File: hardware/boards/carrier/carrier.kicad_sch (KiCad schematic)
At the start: 21 parts, among them J1 XT30PW(2+2), U2 LM5163DDAR

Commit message: Add INA bypass and CAN differential pair rules
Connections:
- net CANH_BUS renamed CAN_BUS_P
- net CANL_BUS renamed CAN_BUS_N
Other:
- sheet Protected Power and Controls ports: added CAN_BUS_N, CAN_BUS_P; removed CANH_BUS, CANL_BUS
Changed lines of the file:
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@@
 		)
 	)
-	(label "CANL_BUS"
+	(label "CAN_BUS_N"
 		(at 180 205.56 180)
 		(effects
@@
 		)
 	)
-	(label "CANL_BUS"
+	(label "CAN_BUS_N"
 		(at 39.37 52.07 180)
 		(effects
@@
 		)
 	)
-	(label "CANH_BUS"
+	(label "CAN_BUS_P"
 		(at 180 210.64 180)
 		(effects
@@
 		)
 	)
-	(label "CANH_BUS"
+	(label "CAN_BUS_P"
 		(at 39.37 54.61 180)
 		(effects
@@
 		)
 	)
-	(label "CANH_BUS"
+	(label "CAN_BUS_P"
 		(at 66.04 41.91 180)
 		(effects
@@
 		)
 	)
-	(label "CANL_BUS"
+	(label "CAN_BUS_N"
 		(at 66.04 64.77 180)
 		(effects
@@
 			)
 		)
-		(pin "CANL_BUS" bidirectional
+		(pin "CAN_BUS_N" bidirectional
 			(at 180 205.56 180)
 			(effects
@@
 			)
 		)
-		(pin "CANH_BUS" bidirectional
+		(pin "CAN_BUS_P" bidirectional
 			(at 180 210.64 180)
 			(effects

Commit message: Checkpoint updated carrier placement and CAN routing
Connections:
- net CAN_BUS_N: now also J1.4 (Pin_4); no longer J1.3 (Pin_3)
- net CAN_BUS_P: now also J1.3 (Pin_3); no longer J1.4 (Pin_4)
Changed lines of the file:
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@@
+		)
+	)
+	(label "CAN_BUS_N"
+		(at 39.37 54.61 180)
+		(effects
+			(font
+				(size 1.27 1.27)
+			)
+			(justify right bottom)
 		)
 	)
@@
 		)
 	)
-	(label "CAN_BUS_N"
-		(at 39.37 52.07 180)
-		(effects
-			(font
-				(size 1.27 1.27)
-			)
-			(justify right bottom)
-		)
-	)
 	(label "BUCK_FB"
 		(at 58.42 161.29 0)
@@
 	)
 	(label "CAN_BUS_P"
-		(at 39.37 54.61 180)
-		(effects
-			(font
-				(size 1.27 1.27)
-			)
-			(justify right bottom)
-		)
-	)
-	(label "CAN_BUS_P"
 		(at 66.04 41.91 180)
 		(effects
@@
 		(effects
 			(font
+				(size 1.27 1.27)
+			)
+			(justify right bottom)
+		)
+	)
+	(label "CAN_BUS_P"
+		(at 39.37 52.07 180)
+		(effects
+			(font

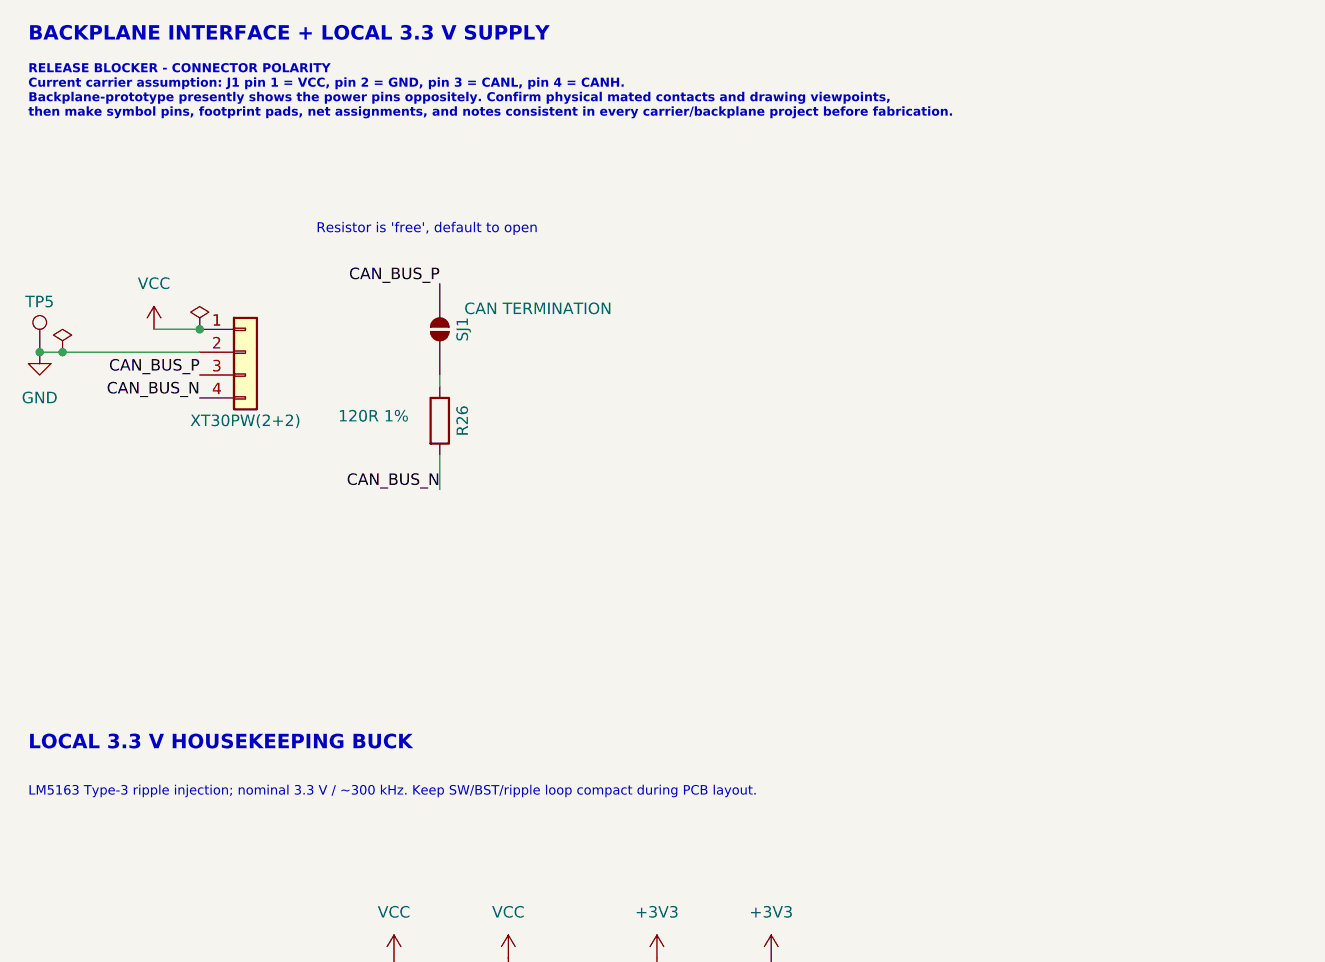
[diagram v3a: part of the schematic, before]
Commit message: Add 0.20 mm-clearance MSOP-10 footprint
Use a project-local MSOP-10 footprint for U3, document the 2 oz fabrication rationale, and include the pending carrier CAN, LED resistor, and choke footprint updates.
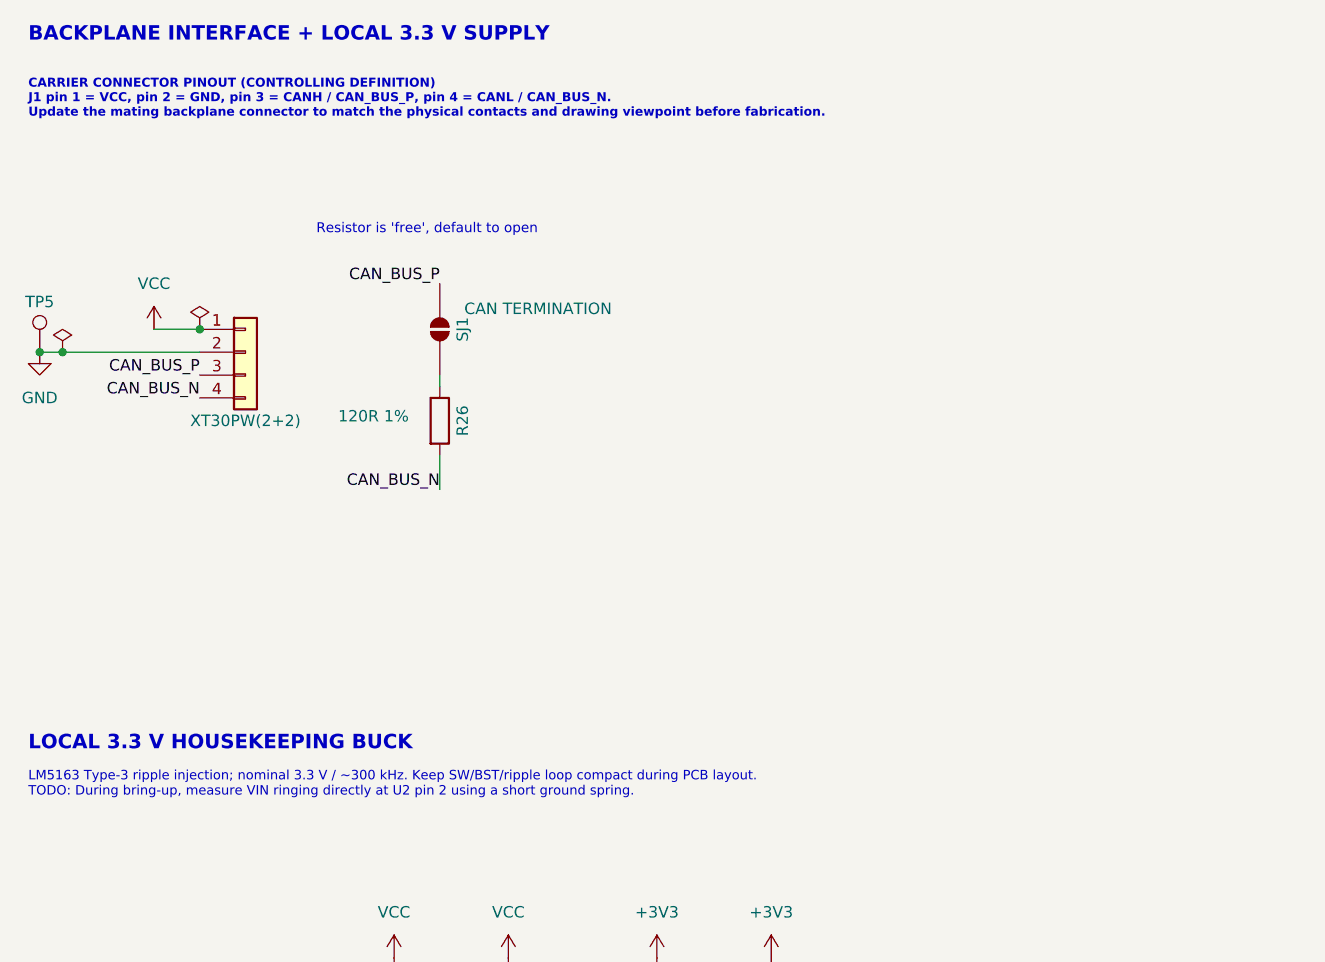
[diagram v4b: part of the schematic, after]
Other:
- note added: "CARRIER CONNECTOR PINOUT (CONTROLLING DEFINITION) J1 pin 1 = VCC, pin 2 = GND, pin 3 = CANH / CAN_BUS_P, pin 4 = CANL / CAN_BUS_N. Update the mating backplane connector to match the physical contacts and drawing viewpoint before fabrication."
- note added: "LM5163 Type-3 ripple injection; nominal 3.3 V / ~300 kHz. Keep SW/BST/ripple loop compact during PCB layout. TODO: During bring-up, measure VIN ringing directly at U2 pin 2 using a short ground spring."
- note removed: "LM5163 Type-3 ripple injection; nominal 3.3 V / ~300 kHz. Keep SW/BST/ripple loop compact during PCB layout."
- note removed: "RELEASE BLOCKER - CONNECTOR POLARITY Current carrier assumption: J1 pin 1 = VCC, pin 2 = GND, pin 3 = CANL, pin 4 = CANH. Backplane-prototype presently shows the power pins oppositely. Confirm physical mated contacts and drawing viewpoints, then make symbol pins, footprint pads, net assignments, and notes consistent in every carrier/backplane project before fabrication."
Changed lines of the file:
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@@
 		)
 	)
-	(text "LM5163 Type-3 ripple injection; nominal 3.3 V / ~300 kHz. Keep SW/BST/ripple loop compact during PCB layout."
+	(text "LM5163 Type-3 ripple injection; nominal 3.3 V / ~300 kHz. Keep SW/BST/ripple loop compact during PCB layout.\nTODO: During bring-up, measure VIN ringing directly at U2 pin 2 using a short ground spring."
 		(exclude_from_sim no)
 		(at 20.32 99.06 0)
@@
 		)
 	)
-	(text "RELEASE BLOCKER - CONNECTOR POLARITY\nCurrent carrier assumption: J1 pin 1 = VCC, pin 2 = GND, pin 3 = CANL, pin 4 = CANH.\nBackplane-prototype presently shows the power pins oppositely. Confirm physical mated contacts and drawing viewpoints,\nthen make symbol pins, footprint pads, net assignments, and notes consistent in every carrier/backplane project before fabrication."
+	(text "CARRIER CONNECTOR PINOUT (CONTROLLING DEFINITION)\nJ1 pin 1 = VCC, pin 2 = GND, pin 3 = CANH / CAN_BUS_P, pin 4 = CANL / CAN_BUS_N.\nUpdate the mating backplane connector to match the physical contacts and drawing viewpoint before fabrication."
 		(exclude_from_sim no)
 		(at 20.32 23.622 0)

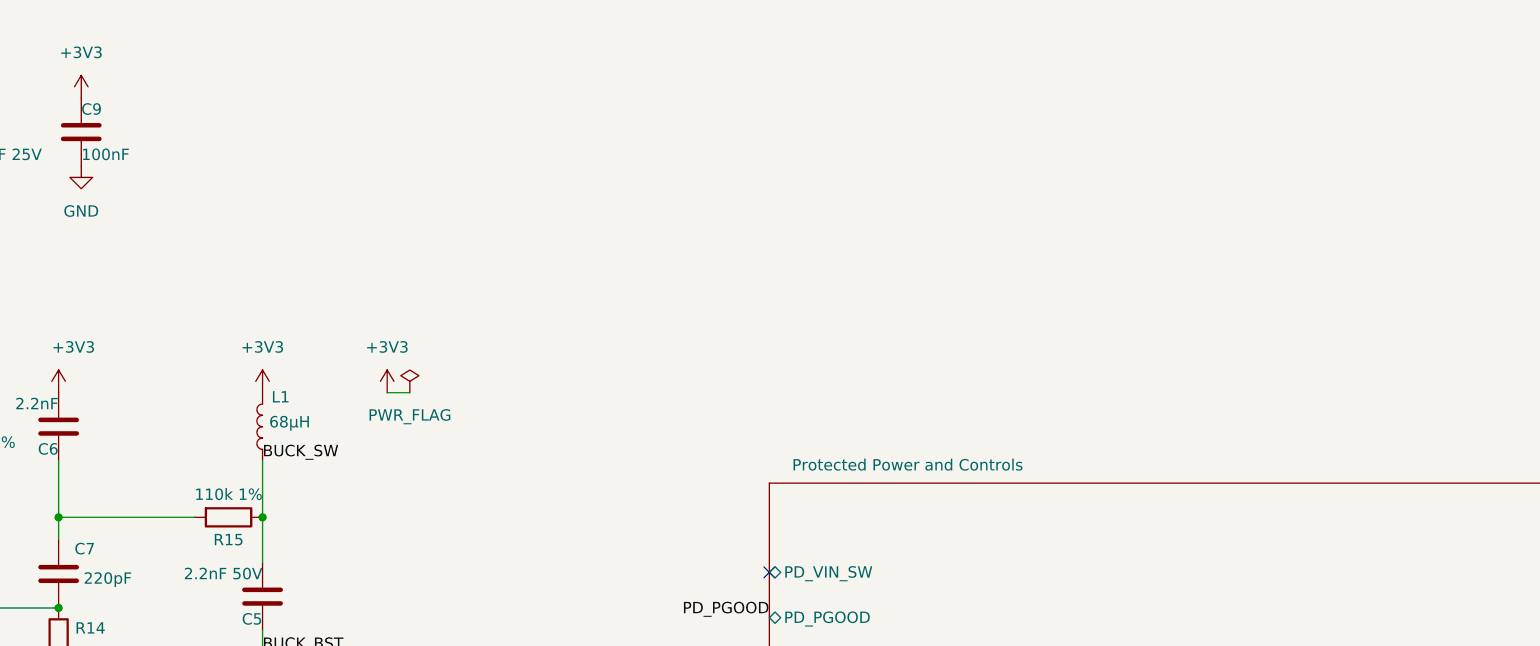
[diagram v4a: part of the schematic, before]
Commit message: add carrier bring-up testpoints
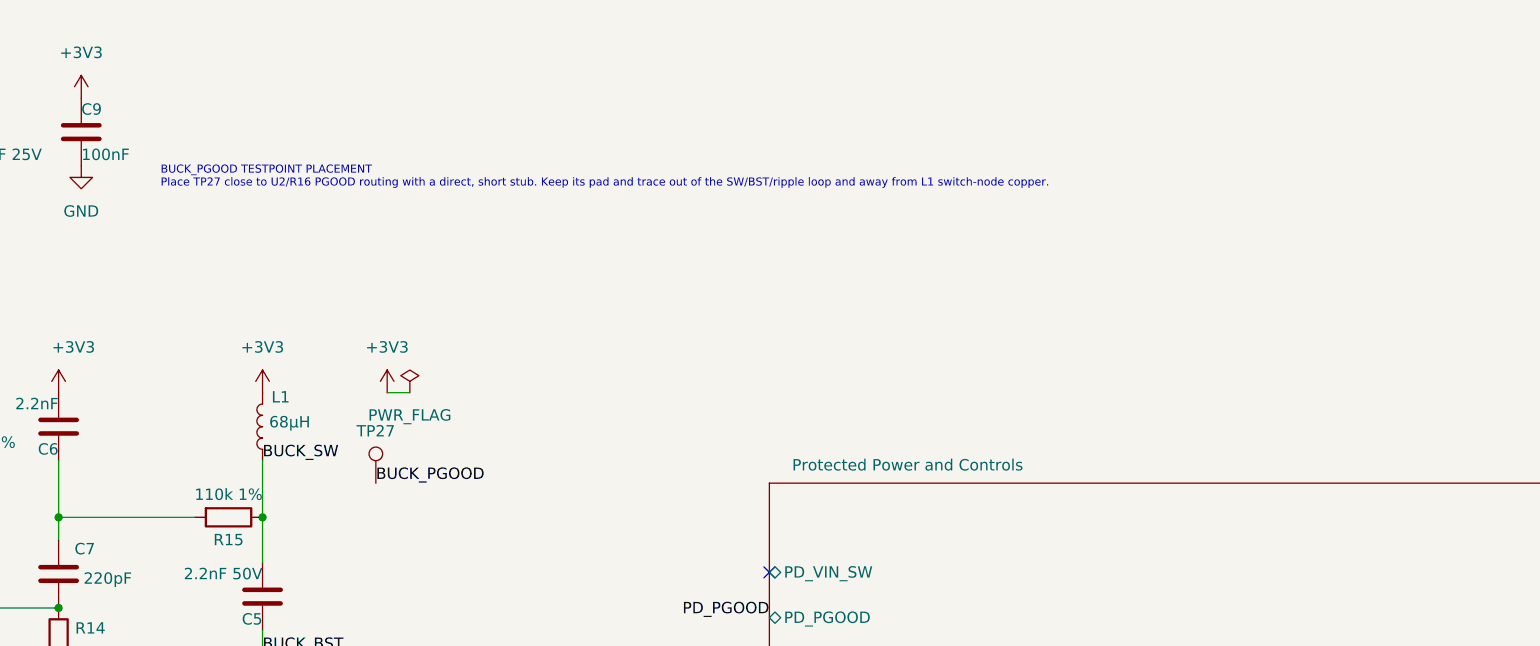
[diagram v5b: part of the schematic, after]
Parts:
- added TP27: BUCK_PGOOD, TestPoint:TestPoint_Pad_D1.5mm, symbol Connector:TestPoint
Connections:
- net BUCK_PGOOD: now also TP27.1
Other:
- note added: "BUCK_PGOOD TESTPOINT PLACEMENT Place TP27 close to U2/R16 PGOOD routing with a direct, short stub. Keep its pad and trace out of the SW/BST/ripple loop and away from L1 switch-node copper."
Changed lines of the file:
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@@
+		)
+	)
+	(text "BUCK_PGOOD TESTPOINT PLACEMENT\nPlace TP27 close to U2/R16 PGOOD routing with a direct, short stub. Keep its pad and trace out of the SW/BST/ripple loop and away from L1 switch-node copper."
+		(exclude_from_sim no)
+		(at 111.76 127 0)
+		(effects
+			(font
+				(size 0.9 0.9)
+			)
+			(justify left bottom)
+		)
+	)
+	(label "BUCK_PGOOD"
+		(at 135.89 160.02 0)
+		(effects
+			(font
+				(size 1.27 1.27)
+			)
+			(justify left bottom)
+		)
+	)
+	(symbol
+		(lib_id "Connector:TestPoint")
+		(at 135.89 160.02 0)
+		(mirror y)
+		(unit 1)
+		(body_style 1)
+		(exclude_from_sim no)
+		(in_bom yes)
+		(on_board yes)
+		(in_pos_files yes)
+		(dnp no)
+		(property "Reference" "TP27"
+			(at 135.89 154.178 0)
+			(show_name no)
+			(do_not_autoplace no)
+			(effects
+				(font
+					(size 1.27 1.27)
+				)
+			)
+		)
+		(property "Value" "BUCK_PGOOD"
+			(at 135.89 143.51 0)
+			(hide yes)
+			(show_name no)
+			(do_not_autoplace no)
+			(effects
+				(font
+					(size 1.27 1.27)
+				)
+			)
+		)
+		(property "Footprint" "TestPoint:TestPoint_Pad_D1.5mm"
+			(at 130.81 160.02 0)
+			(hide yes)
+			(show_name no)
+			(do_not_autoplace no)
+			(effects
+				(font
+					(size 1.27 1.27)
+				)
+			)
+		)
+		(property "Datasheet" ""
+			(at 130.81 160.02 0)
+			(hide yes)
+			(show_name no)
+			(do_not_autoplace no)
+			(effects
+				(font
+					(size 1.27 1.27)
+				)
+			)
+		)
+		(property "Description" "test point"
+			(at 135.89 160.02 0)
+			(hide yes)
+			(show_name no)
+			(do_not_autoplace no)
+			(effects
+				(font
+					(size 1.27 1.27)
+				)
+			)
+		)
+		(property "MPN" "PCB test point"
+			(at 135.89 160.02 0)
+			(hide yes)
+			(show_name no)
+			(do_not_autoplace no)
+			(effects
+				(font
+					(size 1.27 1.27)
+				)
+			)
+		)
+		(property "Package" "1.5 mm SMD pad"
+			(at 135.89 160.02 0)
+			(hide yes)
+			(show_name no)
+			(do_not_autoplace no)
+			(effects
+				(font
+					(size 1.27 1.27)
+				)
+			)
+		)
+		(property "Population" "PCB"
+			(at 135.89 160.02 0)
+			(hide yes)
+			(show_name no)
+			(do_not_autoplace no)
+			(effects
+				(font
+					(size 1.27 1.27)
+				)
+			)
+		)
+		(pin "1"
+		)
+		(instances
+			(project "carrier"
+				(path "/ee42a069-09cc-4091-bee3-2dd6ab96c98c"
+					(reference "TP27")
+					(unit 1)
+				)
+			)
 		)
 	)

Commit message: assign carrier LCSC assembly parts
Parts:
- C3, C4: LCSC (none) -> C55151; MPN (none) -> CL32B225KCJSNNE; Manufacturer (none) -> Samsung Electro-Mechanics
- C5: LCSC (none) -> C1604; MPN (none) -> 0603B222K500NT; Manufacturer (none) -> FH (Guangdong Fenghua Advanced Tech)
- C6: LCSC (none) -> C33353; MPN (none) -> CL10C222JB8NNNC; Manufacturer (none) -> Samsung Electro-Mechanics
- C7: LCSC (none) -> C106210; MPN (none) -> CC0603JRNPO9BN221; Manufacturer (none) -> YAGEO
- C8: LCSC (none) -> C45783; MPN (none) -> CL21A226MAQNNNE; Manufacturer (none) -> Samsung Electro-Mechanics
- C9: LCSC (none) -> C14663; MPN (none) -> CC0603KRX7R9BB104; Manufacturer (none) -> YAGEO
- J1: LCSC (none) -> C19268030
- R12: LCSC (none) -> C22964; MPN (none) -> 0603WAF2742T5E; Manufacturer (none) -> UNI-ROYAL (Uniroyal Elec)
- R13, R15: LCSC (none) -> C25805; MPN (none) -> 0603WAF1103T5E; Manufacturer (none) -> UNI-ROYAL (Uniroyal Elec)
- R14: LCSC (none) -> C23221; MPN (none) -> 0603WAF6202T5E; Manufacturer (none) -> UNI-ROYAL (Uniroyal Elec)
- R16: LCSC (none) -> C25804; MPN (none) -> 0603WAF1002T5E; Manufacturer (none) -> UNI-ROYAL (Uniroyal Elec)

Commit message: use stocked MCU and termination resistor parts
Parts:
- R26: LCSC C114640 -> C22787; MPN RC0603FR-07120RL -> 0603WAF1200T5E; Manufacturer (none) -> UNI-ROYAL (Uniroyal Elec)
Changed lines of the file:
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@@
 			)
 		)
-		(property "MPN" "RC0603FR-07120RL"
+		(property "MPN" "0603WAF1200T5E"
 			(at 66.04 57.15 0)
 			(hide yes)
@@
 			)
 		)
-		(property "LCSC" "C114640"
+		(property "Manufacturer" "UNI-ROYAL (Uniroyal Elec)"
 			(at 66.04 57.15 0)
 			(hide yes)
+			(show_name no)
+			(do_not_autoplace no)
+			(effects
+				(font
+					(size 1.27 1.27)
+				)
+			)
+		)
+		(property "LCSC" "C22787"
+			(at 66.04 57.15 0)
+			(hide yes)
